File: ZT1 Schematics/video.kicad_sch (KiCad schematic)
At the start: 36 parts, among them Q101 2N3904, U129 74LS93, U131 74LS08, U132 74LS10, U133 74LS86, U134 8275, U135 TMS2516, U136 74LS04, U137 74LS175, U138 74ALS574, U139 7409, U141 74LS166, U147 74LS193, U148 74LS193

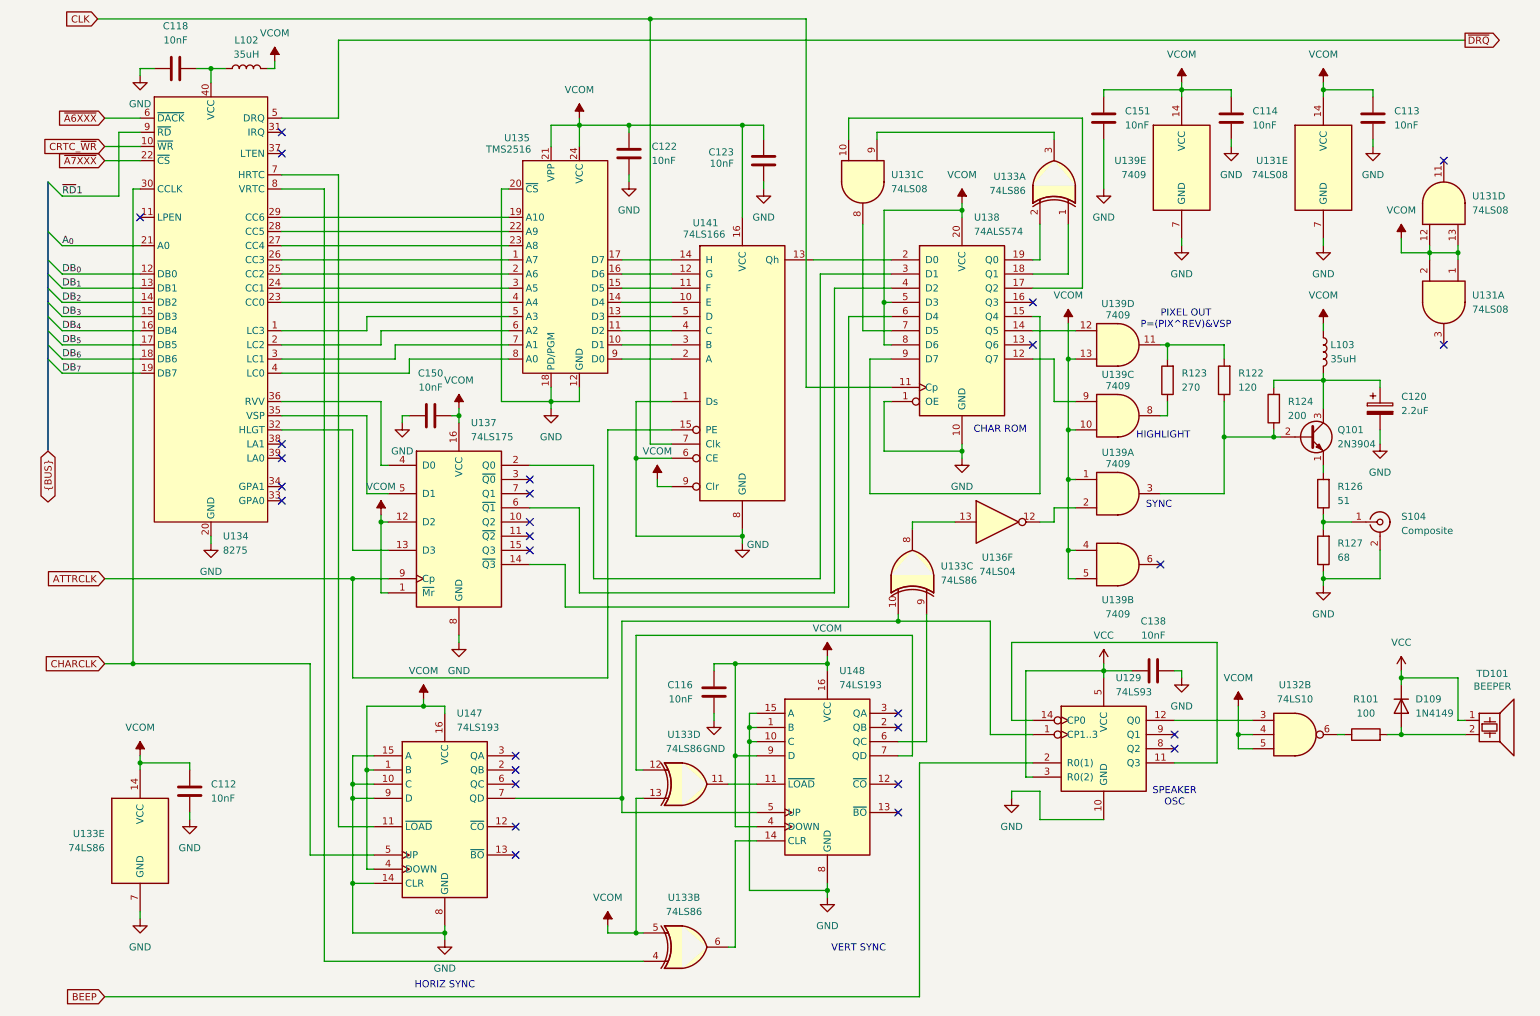
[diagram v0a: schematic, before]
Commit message: Minor touchups
Fixed some of the text
Added some explanations
Simplified the video circuit
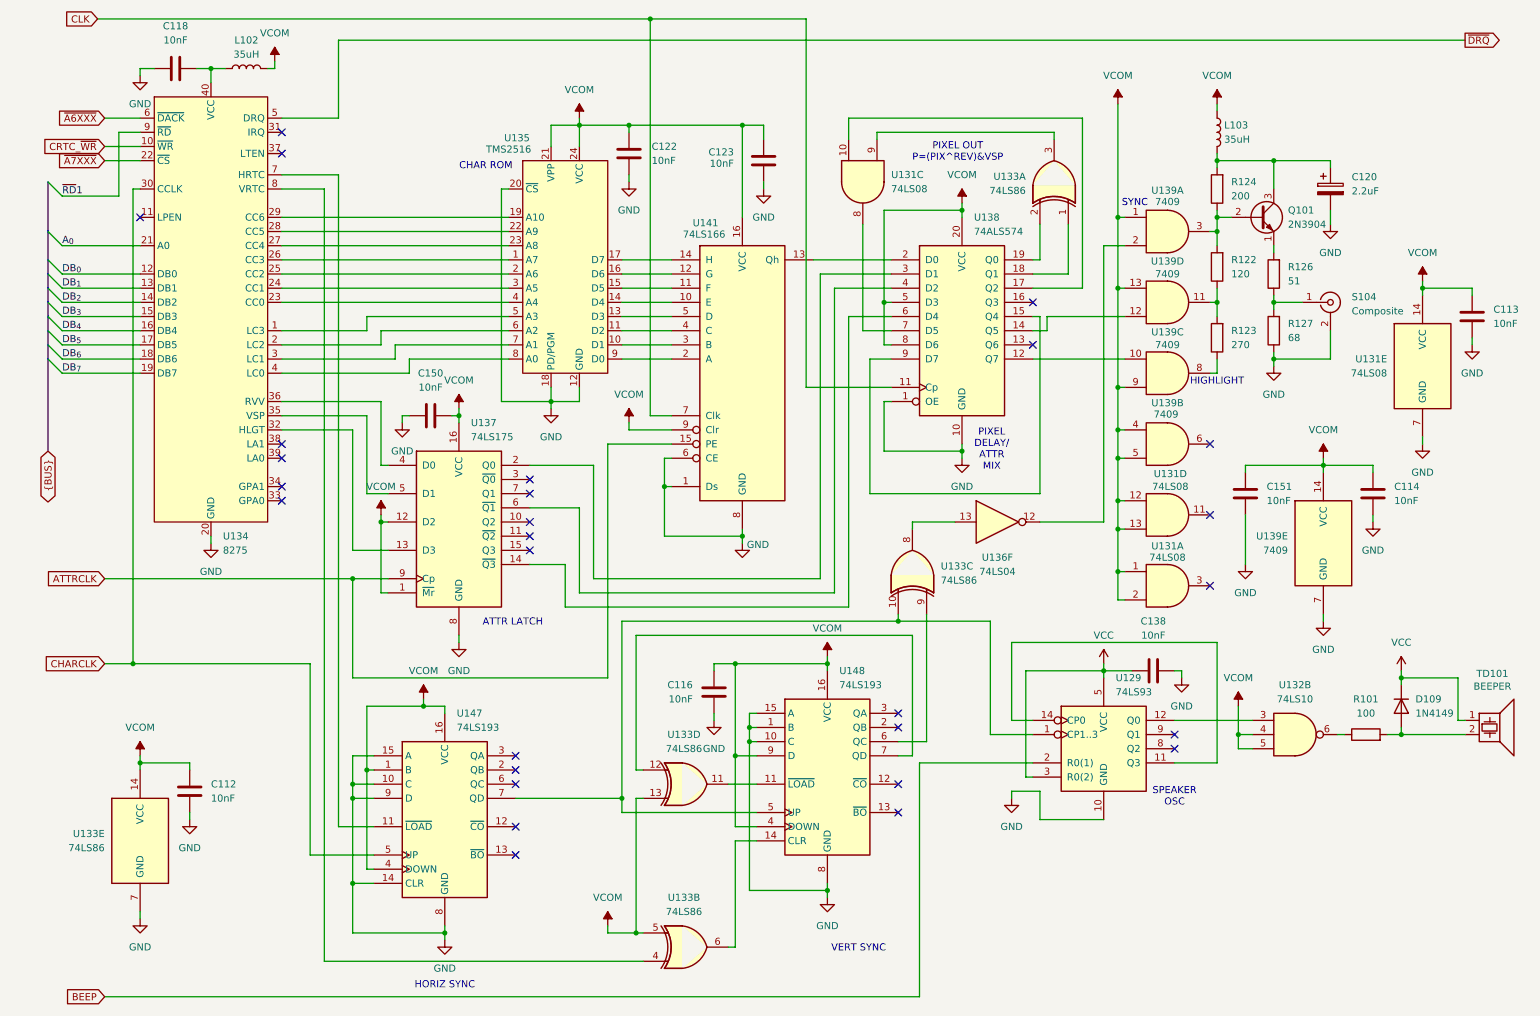
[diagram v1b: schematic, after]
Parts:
- C112, C113, C114, C116, C118, C122, C123, C138, C150, C151: footprint ZX1:C_350mil -> ZT1:C_350mil
- C120: footprint ZX1:CP_520mil -> ZT1:CP_520mil
- D109: footprint ZX1:D_350mil -> ZT1:D_350mil
- L102, L103: footprint ZX1:L_Axial_L7.0mm_D3.3mm_P5.08mm_Vertical_Fastron_MICC -> ZT1:L_Axial_L7.0mm_D3.3mm_P5.08mm_Vertical_Fastron_MICC
- Q101: footprint Package_TO_SOT_THT:TO-92L_Inline_Wide -> Package_TO_SOT_THT:TO-92_Inline
- R101, R122, R123, R124, R126, R127: footprint ZX1:R_450mil -> ZT1:R_450mil
- S104: footprint ZX1:RCA -> ZT1:RCA
- U134: symbol ZX1:8275 -> ZT1:8275
- U135: symbol ZX1:TMS2516 -> ZT1:TMS2516
- U141: symbol 74xx:74LS166 -> ZT1:74LS166
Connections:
- net VCOM: now also U139.9; no longer U139.10
- net at R123.2, U139.11: now also R122.1; no longer R122.2
- net at U138.12 (Q7): now also U139.10; no longer U139.9
- net at Q101.2 (B), R124.1, U139.3: now also R122.2; no longer R122.1
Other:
- note added: "ATTR LATCH"
- note added: "PIXEL DELAY/ ATTR MIX"
- moved on the sheet: C113, C114, C120, C151, L103, Q101, R122, R123, R124, R126, R127, S104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
